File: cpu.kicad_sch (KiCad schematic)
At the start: 19 parts, among them J1 FTSH-105-01-L-DV-K, J24 HTSW-103-07-G-S, U2 CC1312R1F3RGZR, Y2 OW7EL89CANUXK7YLC-48M

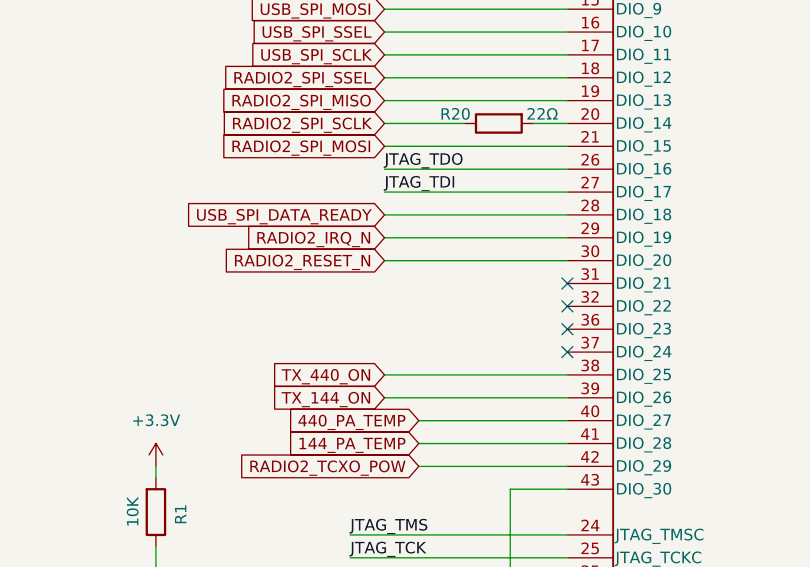
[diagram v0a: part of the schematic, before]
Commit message: Control the 440 switch directly from the CPU
The RX/TX switch on the CC1125 added a lot of complexity with the inverter
and such.  Instead, just drive it frmo the CC1125.

Use the RX/TX switch on the CC1125 as an option shown on the design with
169MHz and an external PA, not populated.

Signed-off-by: Corey Minyard <corey@minyard.net>
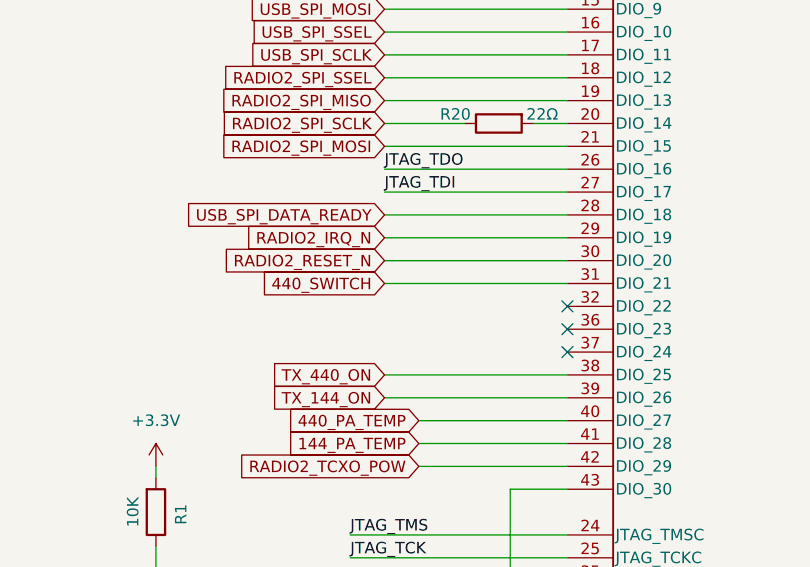
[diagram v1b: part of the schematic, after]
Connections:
- net 440_SWITCH: now reaches U2.31 (DIO_21)
- no-connect marks 8 -> 7
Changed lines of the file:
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@@
 		(at 139.7 143.51)
 	)
-	(no_connect
-		(at 78.74 102.87)
-	)
 	(wire
 		(pts
@@
 		(pts
 			(xy 156.21 80.01) (xy 166.37 80.01)
+		)
+		(stroke
+			(width 0)
+			(type default)
+		)
+	)
+	(wire
+		(pts
+			(xy 58.42 102.87) (xy 78.74 102.87)
 		)
 		(stroke
@@
 			(effects
 				(font
+					(size 1.27 1.27)
+				)
+				(justify right)
+				(hide yes)
+			)
+		)
+	)
+	(global_label "440_SWITCH"
+		(shape input)
+		(at 58.42 102.87 180)
+		(fields_autoplaced yes)
+		(effects
+			(font
+				(size 1.27 1.27)
+			)
+			(justify right)
+		)
+		(property "Intersheetrefs" "${INTERSHEET_REFS}"
+			(at 44.0049 102.87 0)
+			(effects
+				(font

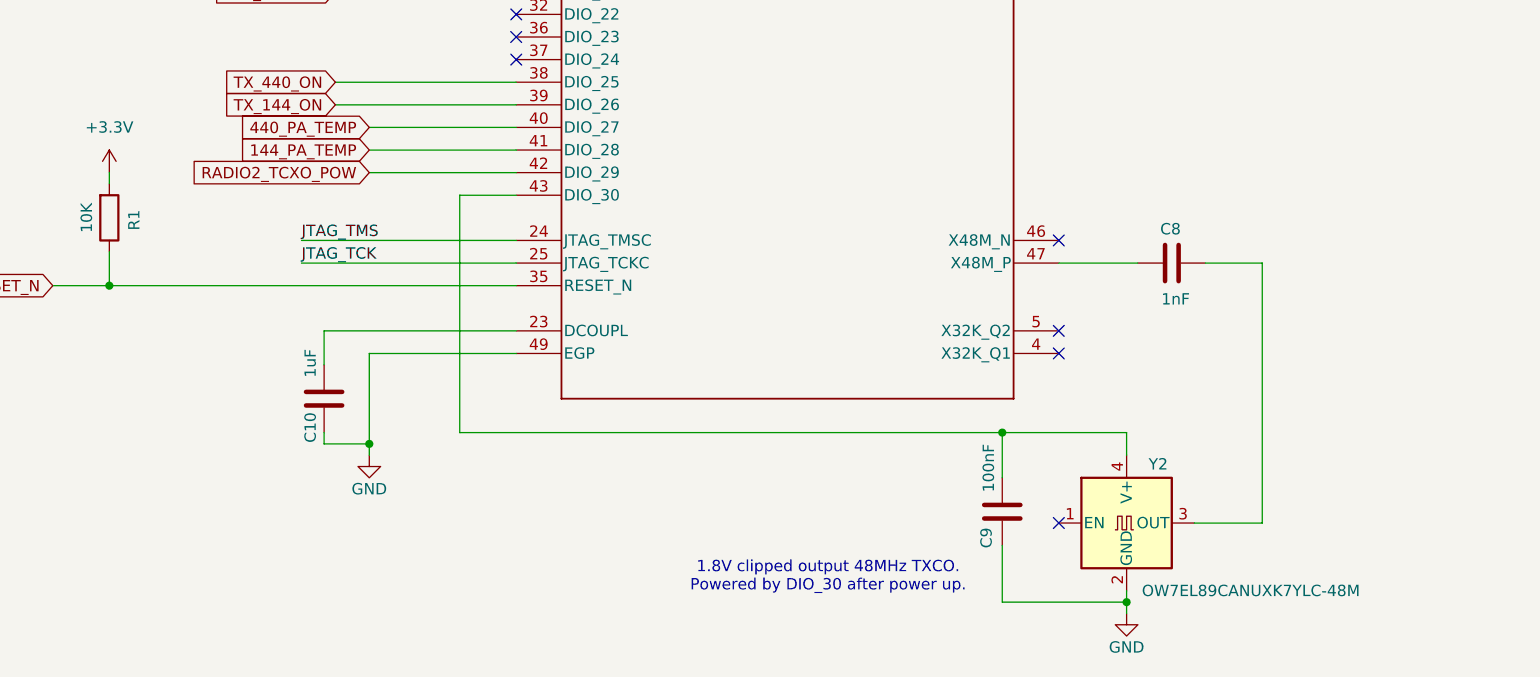
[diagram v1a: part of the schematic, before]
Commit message: Directly power the oscillators
There is only one D/A converter on the CC1312R, so you really couldn't
power both of the oscillators from that chip.  Power is not a concern,
so just directly power them from 3.3V.  That required using a different
oscillator chip, too, but it was available on both frequencies.

Signed-off-by: Corey Minyard <corey@minyard.net>
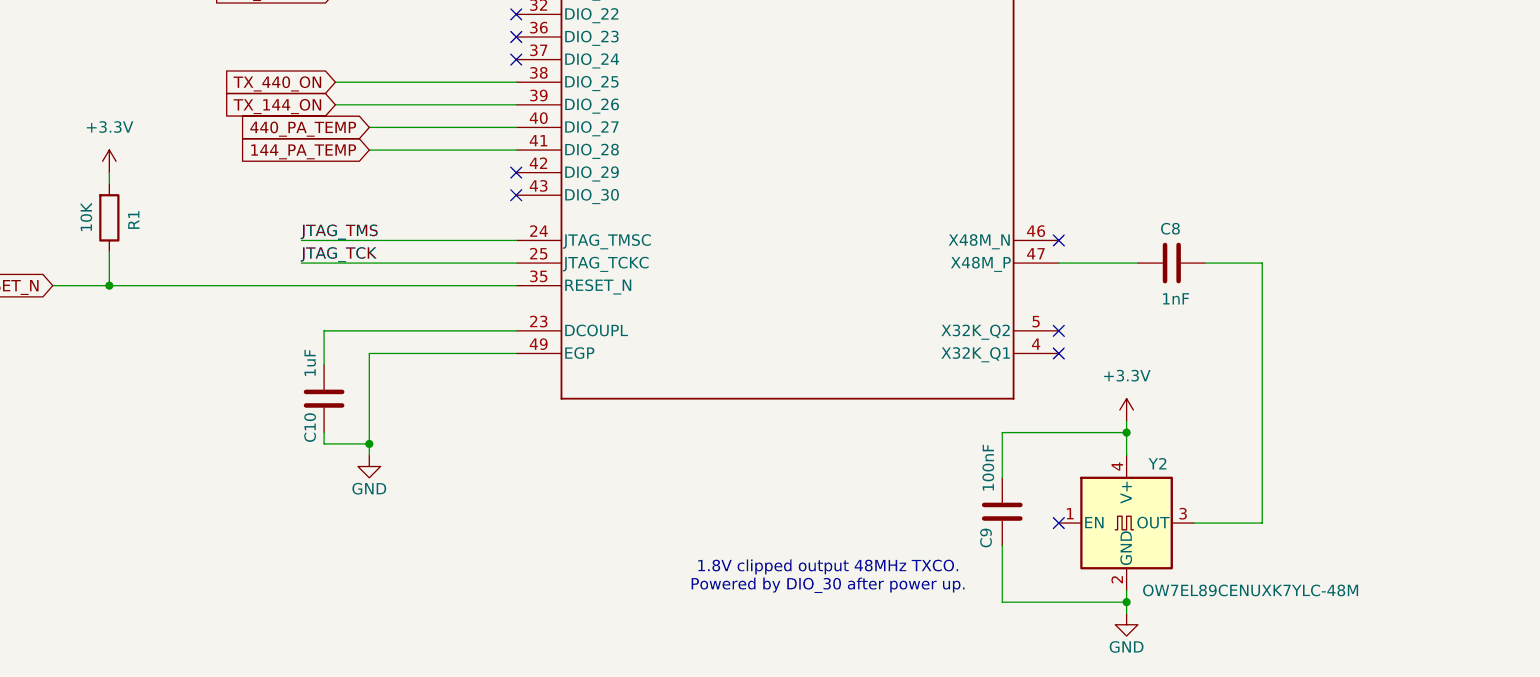
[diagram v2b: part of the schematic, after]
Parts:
- Y2: value OW7EL89CANUXK7YLC-48M -> OW7EL89CENUXK7YLC-48M
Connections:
- net +3.3V: now also C9.2, Y2.4 (V+)
- net RADIO2_TCXO_POW: no longer names the net of U2.42 (DIO_29)
- now unconnected: U2.43 (DIO_30)
- no-connect marks 7 -> 9
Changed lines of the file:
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@@
 	)
 	(junction
-		(at 133.35 152.4)
-		(diameter 0)
-		(color 0 0 0 0)
-	)
-	(junction
 		(at 148.59 54.61)
 		(diameter 0)
@@
 	)
 	(junction
+		(at 147.32 152.4)
+		(diameter 0)
+		(color 0 0 0 0)
+	)
+	(junction
 		(at 182.88 73.66)
 		(diameter 0)
@@
 	)
 	(no_connect
+		(at 78.74 123.19)
+	)
+	(no_connect
 		(at 139.7 143.51)
 	)
+	(no_connect
+		(at 78.74 125.73)
+	)
 	(wire
 		(pts
@@
 	(wire
 		(pts
-			(xy 62.23 123.19) (xy 78.74 123.19)
-		)
-		(stroke
-			(width 0)
-			(type default)
-		)
-	)
-	(wire
-		(pts
 			(xy 213.36 101.6) (xy 220.98 101.6)
 		)
@@
 	(wire
 		(pts
-			(xy 78.74 125.73) (xy 72.39 125.73)
+			(xy 58.42 59.69) (xy 78.74 59.69)
 		)
 		(stroke
@@
 	(wire
 		(pts
-			(xy 58.42 59.69) (xy 78.74 59.69)
+			(xy 180.34 34.29) (xy 180.34 35.56)
 		)
 		(stroke
@@
 	(wire
 		(pts
-			(xy 180.34 34.29) (xy 180.34 35.56)
+			(xy 147.32 151.13) (xy 147.32 152.4)
 		)
 		(stroke
@@
 	(wire
 		(pts
-			(xy 72.39 152.4) (xy 133.35 152.4)
-		)
-		(stroke
-			(width 0)
-			(type default)
-		)
-	)
-	(wire
-		(pts
 			(xy 57.15 140.97) (xy 78.74 140.97)
 		)
@@
 	(wire
 		(pts
-			(xy 72.39 125.73) (xy 72.39 152.4)
-		)
-		(stroke
-			(width 0)
-			(type default)
-		)
-	)
-	(wire
-		(pts
 			(xy 54.61 130.81) (xy 78.74 130.81)
 		)
@@
 		)
 	)
-	(global_label "RADIO2_TCXO_POW"
-		(shape input)
-		(at 62.23 123.19 180)
-		(fields_autoplaced yes)
-		(effects
-			(font
-				(size 1.27 1.27)
-			)
-			(justify right)
-		)
-		(property "Intersheetrefs" "${INTERSHEET_REFS}"
-			(at 41.7067 123.19 0)
-			(effects
-				(font
-					(size 1.27 1.27)
-				)
-				(justify right)
-				(hide yes)
-			)
-		)
-	)
 	(global_label "USB_SPI_DATA_READY"
 		(shape input)
@@
 			)
 		)
-		(property "Value" "OW7EL89CANUXK7YLC-48M"
+		(property "Value" "OW7EL89CENUXK7YLC-48M"
 			(at 161.29 170.18 0)
 			(effects
@@
 					(unit 1)
 				)
+			)
+		)
+	)
+	(symbol
+		(lib_id "power:+3.3V")
+		(at 147.32 151.13 0)
+		(unit 1)
+		(exclude_from_sim no)
+		(in_bom yes)
+		(on_board yes)
+		(dnp no)
+		(fields_autoplaced yes)
+		(property "Reference" "#PWR056"
+			(at 147.32 154.94 0)
+			(effects
+				(font
+					(size 1.27 1.27)
+				)
+				(hide yes)
+			)
+		)
+		(property "Value" "+3.3V"
+			(at 147.32 146.05 0)
+			(effects
+				(font
+					(size 1.27 1.27)
+				)
+			)
+		)
+		(property "Footprint" ""
+			(at 147.32 151.13 0)
+			(effects
+				(font
+					(size 1.27 1.27)
+				)
+				(hide yes)
+			)
+		)
+		(property "Datasheet" ""
+			(at 147.32 151.13 0)
+			(effects
+				(font
+					(size 1.27 1.27)
+				)
+				(hide yes)
+			)
+		)
+		(property "Description" "Power symbol creates a global label with name \"+3.3V\""
+			(at 147.32 151.13 0)
+			(effects
+				(font
+					(size 1.27 1.27)
+				)
+				(hide yes)
+			)
+		)
+		(pin "1"
+		)
+		(instances
+			(project "FSKGroundStation"
+				(path "/23e49ab9-97e0-460a-806c-ff6f37958474/f1de8cbf-f219-47ea-9542-15169289ddba"
+					(reference "#PWR056")
+					(unit 1)
+				)

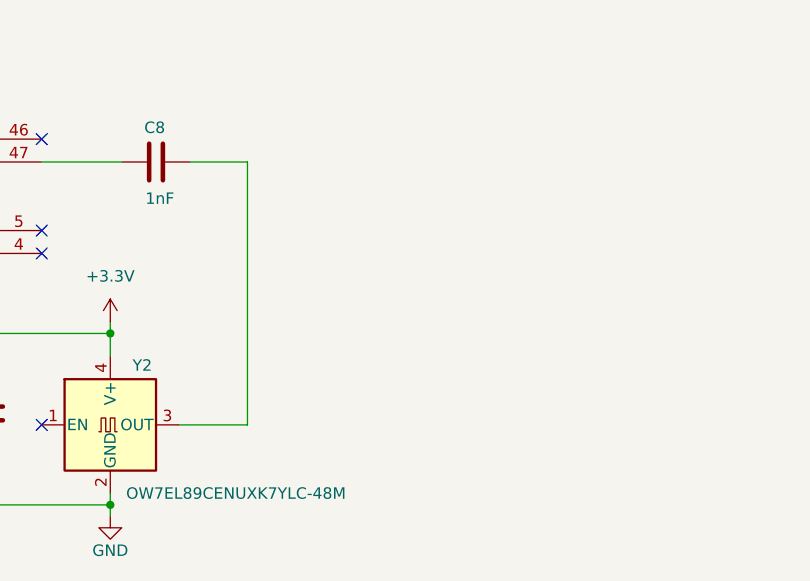
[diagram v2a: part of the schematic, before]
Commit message: Fix some oscillator issues
Ground an unused oscillator line on the CC1125 that needs to be grounded
in external oscillator mode.

Add a resistor divider to the oscillator inputs in case the voltage
needs to be decreased.  It should be fixable with the internal capacitor
tuning, but just in case.

Signed-off-by: Corey Minyard <corey@minyard.net>
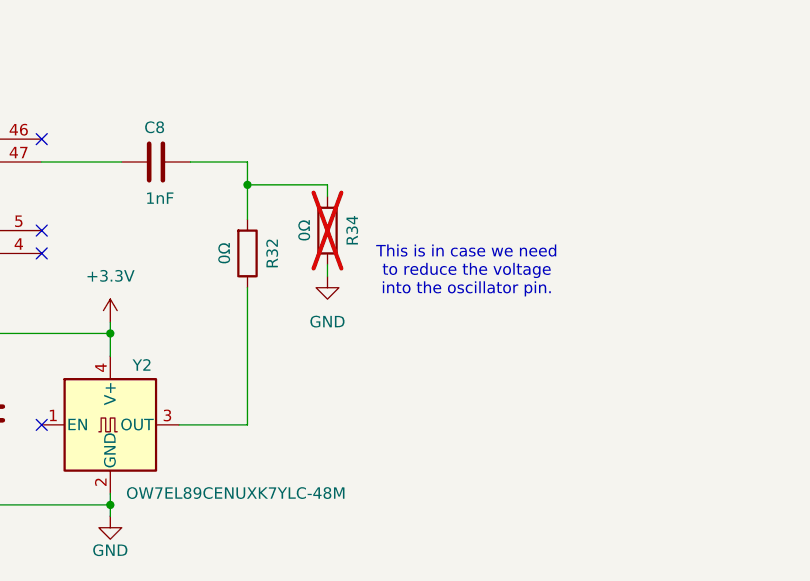
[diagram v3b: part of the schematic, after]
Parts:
- added R32, R34: 0Ω, Resistor_SMD:R_0402_1005Metric, symbol Device:R
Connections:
- net GND: now also R34.1
- net at C8.2: now also R32.2, R34.2; no longer Y2.3 (OUT)
- new net: R32.1, Y2.3 (OUT)
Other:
- note added: "This is in case we need to reduce the voltage into the oscillator pin."

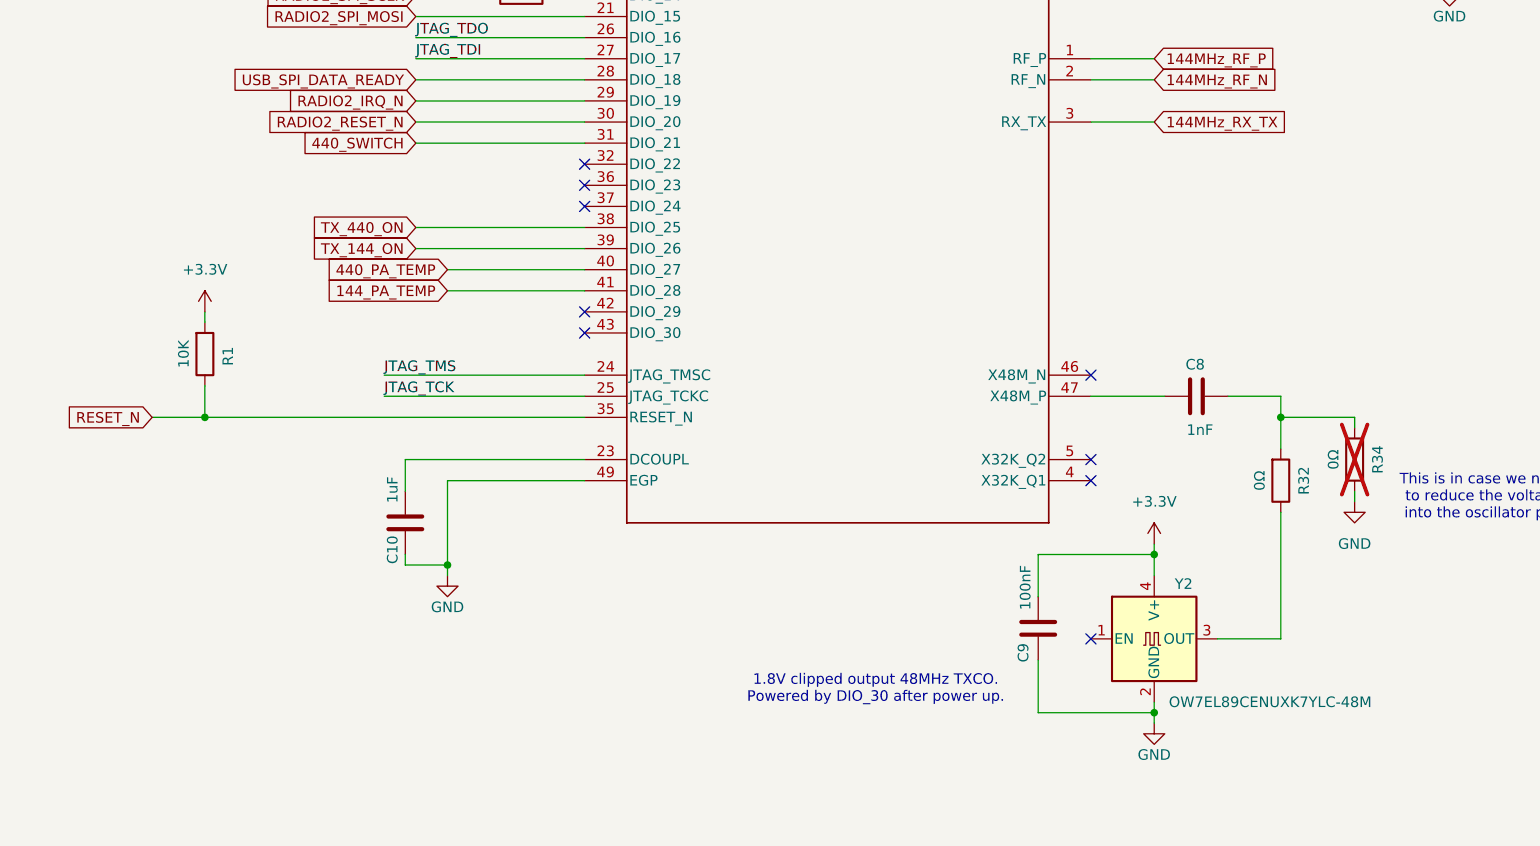
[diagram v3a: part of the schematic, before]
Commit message: Make a bunch of GPIOs more easily available
Put them on DNP zero-ohm resistors.

Signed-off-by: Corey Minyard <corey@minyard.net>
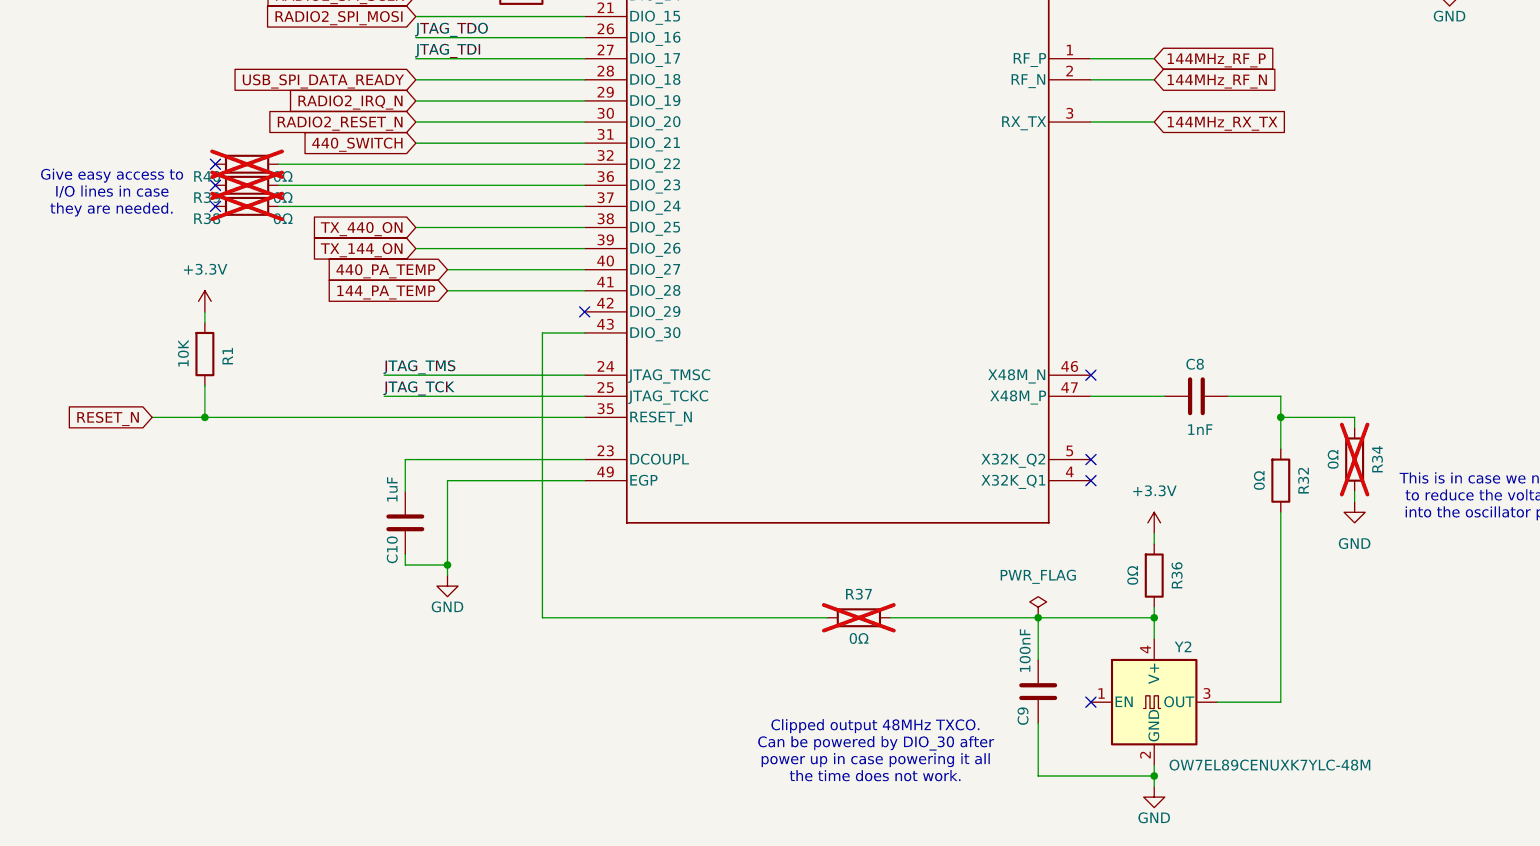
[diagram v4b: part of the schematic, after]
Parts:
- added R36, R37, R38, R39, R40: 0Ω, Resistor_SMD:R_0402_1005Metric, symbol Device:R
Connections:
- net +3.3V: now also R36.2; no longer C9.2, Y2.4 (V+)
- net at U2.32 (DIO_22): now also R40.1
- net at U2.36 (DIO_23): now also R39.1
- net at U2.37 (DIO_24): now also R38.1
- net at U2.43 (DIO_30): now also R37.2
- new net: C9.2, R36.1, R37.1, Y2.4 (V+)
- no-connect marks 9 -> 8
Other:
- note added: "Clipped output 48MHz TXCO. Can be powered by DIO_30 after power up in case powering it all the time does not work."
- note added: "Give easy access to I/O lines in case they are needed."
- note removed: "1.8V clipped output 48MHz TXCO. Powered by DIO_30 after power up."
- moved on the sheet: C9, Y2
